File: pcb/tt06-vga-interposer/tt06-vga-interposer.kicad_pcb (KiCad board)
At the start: 2 copper layers, 55.9 x 53.3 mm, 69 parts, among them CON1 Bottom pins, CON2 Bottom pins, CON3 Top socket, CON4 Top socket, J1 Conn_02x07_Odd_Even, J2 DE15_Receptacle_HighDensity_M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, J3 Conn_01x04_Pin, J4 Conn_01x04_Pin, U1 OPA3355EA, U2 SN74ALVC245DWR

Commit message: Partial layout of interposer PCB
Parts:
- added JP16: SolderJumper_2_Open, Anton Kicad Footprints Lib:SolderJumper-2_tiny_nomask, F.Cu at (88.9, 76.2)
- added JP17: SolderJumper_2_Open, Anton Kicad Footprints Lib:SolderJumper-2_tiny_nomask, F.Cu at (88.9, 81.3)
- added U3: SN74LVC245APW, Anton Kicad Footprints Lib:TSSOP-20_4.4x6.5mm_P0.65mm_HandSolder, F.Cu at (241.0, 68.2)
- C1, C2, JP10, JP11, JP12, JP7, JP8, JP9: moved to B.Cu
- J1: value Conn_02x07_Odd_Even -> Conn_02x09_Odd_Even; footprint Connector_PinHeader_2.54mm:PinHeader_2x07_P2.54mm_Vertical -> Connector_PinHeader_2.54mm:PinHeader_2x09_P2.54mm_Horizontal
- moved U2 147.3 mm to (249.3, 69.2)
- moved J1 133.6 mm to (90.2, 48.3), turned to 90 degrees
- moved TP2 115.8 mm to (92.1, 71.1)
- moved TP3 114.9 mm to (92.7, 83.8)
- moved R304 104.8 mm to (91.4, 89.5), turned to -90 degrees
- moved JP301 104.6 mm to (103.5, 80.0), turned to 180 degrees
- moved R305 100.7 mm to (95.2, 89.5), turned to -90 degrees
- moved NT1 100.6 mm to (112.4, 50.8)
- moved R306 100.6 mm to (102.2, 76.2)
- moved R307 100.0 mm to (102.2, 72.4)
- moved R301 99.4 mm to (96.5, 72.4), turned to 180 degrees
- moved R302 99.4 mm to (96.5, 76.2), turned to 180 degrees
- moved R303 99.4 mm to (96.5, 80.0), turned to 180 degrees
- moved R201 98.9 mm to (90.8, 66.7), turned to 180 degrees
- moved JP101 97.2 mm to (113.0, 96.5), turned to 90 degrees
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- renumbered C9 to C3, C11 to C4, C10 to C5, JP16 to JP201, JP17 to JP301, R310 to R1, R309 to R2, R308 to R3, R35 to R4, R33 to R5
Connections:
- J1 pad 13: GND -> inv_aout
- J1 pad 14: GND -> inv_aout
- JP18 pad 2: Net-(JP18-B) -> /hs_buf
- JP19 pad 2: Net-(JP18-B) -> /vs_buf
- R1 pad 1: Net-(U2-B0) -> /hs_buf
- R2 pad 1: Net-(U2-B0) -> /hs_buf
- R3 pad 1: Net-(JP18-B) -> /vs_buf
- R4 pad 1: Net-(JP18-B) -> /vs_buf
- U2 pad 17: Net-(JP18-B) -> /vs_buf
- U2 pad 18: Net-(U2-B0) -> /hs_buf
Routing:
- net GND: track 181.5 -> 344.2 mm, vias 0 -> 1
- net red_out: track 0.00 -> 106.8 mm, vias 0 -> 1
- net blue_out: track 0.00 -> 104.9 mm, vias 0 -> 3
- net green_out: track 0.00 -> 92.2 mm
- net VCC: track 0.00 -> 80.9 mm, vias 0 -> 2
- net dac4_aout: track 0.00 -> 51.6 mm, vias 0 -> 3
- net inv_aout: track 0.00 -> 45.9 mm, vias 0 -> 2
- net red_in: track 0.00 -> 29.6 mm
- net green_in: track 0.00 -> 28.6 mm
- net blue_in: track 0.00 -> 28.5 mm, vias 0 -> 1
- net Net-(U1B--): track 0.00 -> 25.6 mm
- net Net-(R203-Pad2): track 0.00 -> 23.4 mm
- net Net-(R303-Pad2): track 0.00 -> 16.6 mm, vias 0 -> 2
- net vdda_in: track 0.00 -> 15.4 mm
- net Net-(U1C--): track 0.00 -> 12.1 mm, vias 0 -> 2
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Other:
- board size 55.9 x 53.3 mm -> 67.9 x 62.2 mm
- board text added: "B"
- board text added: "G"
- board text added: "R"
- board text added: "dac4_aout"
- board text added: "inv_aout"

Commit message: Nearly finished 1st draft of interposer PCB
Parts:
- removed the JP13 at (88.9, 86.4)
- removed the JP14 at (88.9, 73.7)
- removed the U2 at (249.3, 69.2)
- added J5: Conn_02x07_Odd_Even, Connector_PinHeader_2.54mm:PinHeader_2x07_P2.54mm_Horizontal, F.Cu at (105.4, 96.5)
- added JP16: SolderJumper_2_Open, Anton Kicad Footprints Lib:SolderJumper-2_tiny_nomask, F.Cu at (93.7, 55.9)
- added NT2: NetTie_2, NetTie:NetTie-2_SMD_Pad0.5mm, F.Cu at (91.2, 57.9)
- added NT3: NetTie_2, NetTie:NetTie-2_SMD_Pad0.5mm, F.Cu at (91.2, 59.4)
- C3, C4: moved to B.Cu
- moved U2 140.6 mm to (100.8, 56.4)
- moved JP18 97.8 mm to (100.6, 55.9)
- moved JP17 97.6 mm to (100.6, 54.4)
- moved C4 62.7 mm to (99.2, 58.4)
- moved C3 59.3 mm to (99.2, 54.6)
- moved R4 57.5 mm to (108.0, 58.9), turned to 90 degrees
- moved R3 37.5 mm to (111.3, 58.9), turned to 90 degrees
- moved JP15 29.9 mm to (93.7, 54.4), turned to 180 degrees
- moved R2 28.5 mm to (111.3, 52.8), turned to 90 degrees
- moved R1 27.4 mm to (108.0, 52.8), turned to 90 degrees
- moved R201 26.3 mm to (99.7, 91.4), turned to -90 degrees
- moved R301 19.1 mm to (95.9, 91.4), turned to -90 degrees
- moved R304 18.0 mm to (92.1, 71.5), turned to 90 degrees
- moved R305 18.0 mm to (95.9, 71.5), turned to 90 degrees
- moved TP2 17.6 mm to (99.7, 87.0)
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- renumbered JP16 to JP13, JP17 to JP14, JP18 to JP17, JP19 to JP18, U3 to U2
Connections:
- net vsync_in renamed Net-(JP16-A)
- J1 pad 1: VCC -> GND
- J1 pad 10: hsync_out -> vsync_out
- J1 pad 11: vsync_out -> blue_out
- J1 pad 12: vsync_out -> blue_out
- J1 pad 13: inv_aout -> green_out
- J1 pad 14: inv_aout -> green_out
- J1 pad 15: dac4_aout -> red_out
- J1 pad 16: dac4_aout -> red_out
- J1 pad 17: GND -> VCC
- J1 pad 18: GND -> VCC
- J1 pad 2: VCC -> GND
- J1 pad 3: red_out -> inv_aout
- J1 pad 4: red_out -> inv_aout
- J1 pad 5: green_out -> dac4_aout
- J1 pad 6: green_out -> dac4_aout
- J1 pad 7: blue_out -> hsync_out
- J1 pad 8: blue_out -> hsync_out
- J1 pad 9: hsync_out -> vsync_out
- JP15 pad 1: /chip_an4 -> Net-(JP15-A)
- JP15 pad 2: blue_in -> hsync_in
- JP17 pad 1: hsync_in -> Net-(JP15-A)
- U2 pad 2: hsync_in -> Net-(JP15-A)
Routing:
- net GND: track 344.2 -> 595.6 mm, vias 1 -> 10
- net hsync_out: track 2.54 -> 67.8 mm
- net vsync_out: track 2.54 -> 64.8 mm, vias 0 -> 1
- net /chip_an0: track 7.27 -> 46.5 mm, vias 0 -> 1
- net red_out: track 106.8 -> 75.9 mm
- net green_out: track 92.2 -> 63.3 mm
- net /chip_an5: track 7.27 -> 33.5 mm, vias 0 -> 1
- net /chip_an4: track 7.27 -> 32.4 mm, vias 0 -> 1
- net blue_out: track 104.9 -> 81.3 mm, vias 3 -> 1
- net Net-(U1B--): track 25.6 -> 7.58 mm
- net dac4_aout: track 51.6 -> 37.9 mm, vias 3 -> 1
- net /vs_buf: track 0.00 -> 13.5 mm
- net red_in: track 29.6 -> 16.3 mm
- net inv_aout: track 45.9 -> 32.9 mm, vias 2 -> 1
- net /hs_buf: track 0.00 -> 10.4 mm
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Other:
- board size 67.9 x 62.2 mm -> 67.3 x 62.2 mm

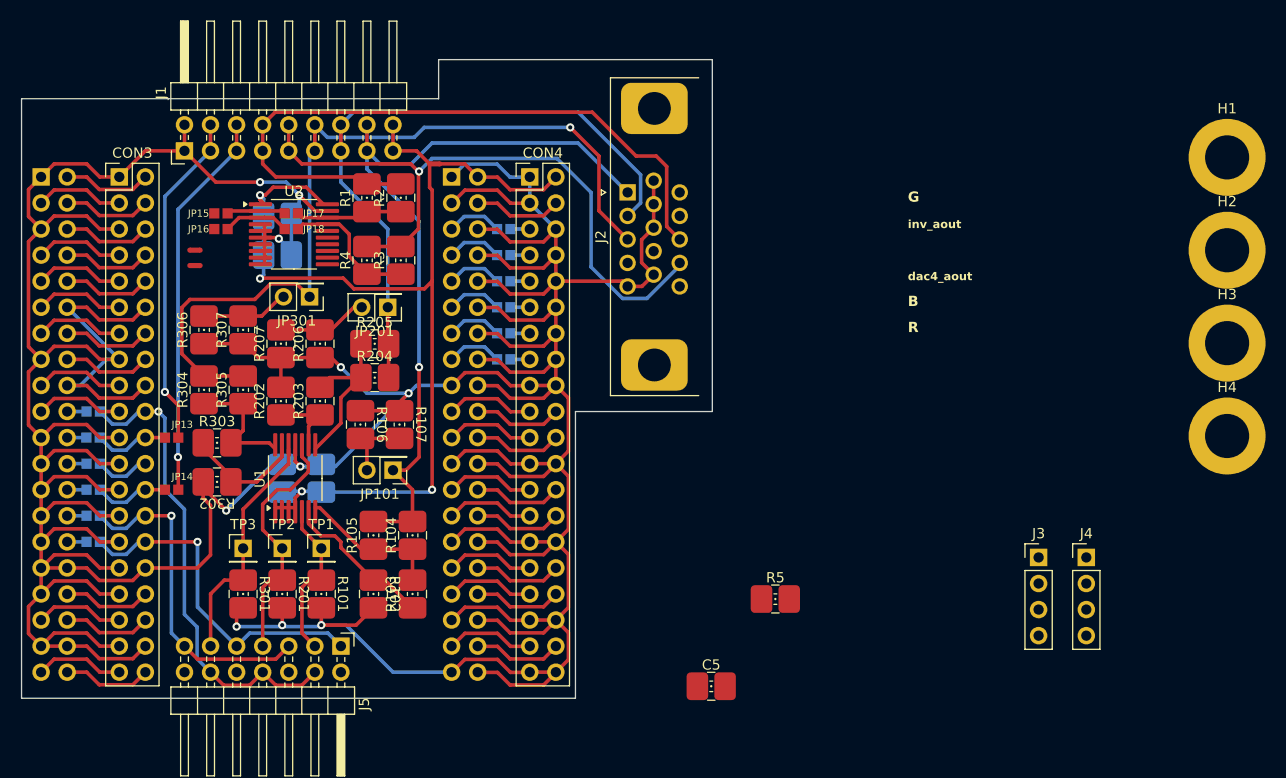
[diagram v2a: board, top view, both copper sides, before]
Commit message: Interposer PCB: First complete version
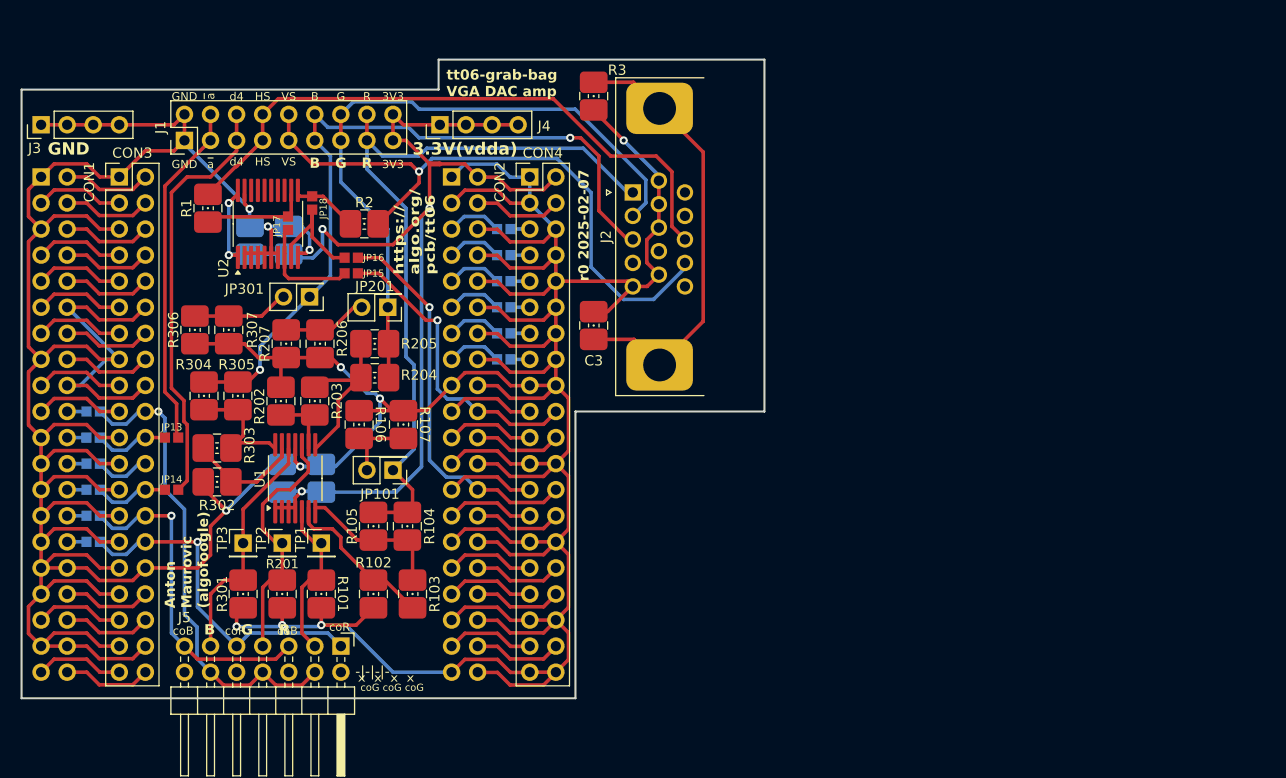
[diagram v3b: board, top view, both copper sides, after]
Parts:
- removed H1, H2, H3, H4: MountingHole, MountingHole:MountingHole_4.3mm_M4_DIN965_Pad
- removed NT2, NT3: NetTie_2, NetTie:NetTie-2_SMD_Pad0.5mm
- removed the R3 at (111.3, 58.9)
- removed R4: 100, Anton Kicad Footprints Lib:SMD_Passive_HandSolder_0603_to_1210
- J1: footprint Connector_PinHeader_2.54mm:PinHeader_2x09_P2.54mm_Horizontal -> Connector_PinHeader_2.54mm:PinHeader_2x09_P2.54mm_Vertical
- R1, R2: value 100 -> 49.9
- moved J3 105.9 mm to (76.2, 45.7), turned to 90 degrees
- moved J4 75.8 mm to (115.1, 45.7), turned to 90 degrees
- moved R3 52.1 mm to (130.0, 42.9), turned to -90 degrees
- moved C3 37.0 mm to (130.0, 65.3), turned to 90 degrees
- moved R1 15.5 mm to (92.5, 53.8)
- moved JP15 14.0 mm to (106.4, 60.2), turned to 0 degrees
- moved JP16 13.0 mm to (106.4, 58.7), turned to 0 degrees
- moved R2 4.37 mm to (107.7, 55.4), turned to 0 degrees
- moved C4 3.56 mm to (96.6, 57.0), turned to 90 degrees
- moved JP18 3.25 mm to (102.6, 53.3), turned to 90 degrees
- moved U2 2.74 mm to (98.3, 55.4), turned to 90 degrees
- moved C5 1.81 mm to (100.3, 57.0), turned to 90 degrees
- moved R307 1.40 mm to (94.5, 65.7)
- moved R104 1.02 mm to (111.9, 84.8)
- moved J1 1.02 mm to (90.2, 47.2)
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- renumbered C5 to C3, C3 to C4, C4 to C5, R5 to R3
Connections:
- JP15 pad 1: Net-(JP15-A) -> hsync_in
- JP15 pad 2: hsync_in -> /uout7
- JP16 pad 1: Net-(JP16-A) -> vsync_in
- JP16 pad 2: vsync_in -> /uout3
- JP17 pad 1: Net-(JP15-A) -> hsync_in
- JP18 pad 1: Net-(JP16-A) -> vsync_in
- R2 pad 1: /hs_buf -> /vs_buf
- R2 pad 2: hsync_out -> vsync_out
- U2 pad 11: unconnected-(U2-B8-Pad11) -> /vs_buf
- U2 pad 12: unconnected-(U2-B7-Pad12) -> /hs_buf
- U2 pad 17: /vs_buf -> unconnected-(U2-B2-Pad17)
- U2 pad 18: /hs_buf -> unconnected-(U2-B1-Pad18)
- U2 pad 2: Net-(JP15-A) -> GND
- U2 pad 3: Net-(JP16-A) -> GND
- U2 pad 8: GND -> hsync_in
- U2 pad 9: GND -> vsync_in
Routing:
- net Net-(C3-Pad1): track 0.00 -> 43.4 mm
- net /uout3: track 8.63 -> 38.4 mm, vias 0 -> 1
- net GND: track 595.6 -> 620.1 mm, vias 10 -> 11
- net /uout7: track 8.63 -> 29.8 mm, vias 0 -> 1
- net vsync_in: track 0.00 -> 11.7 mm
- net hsync_in: track 0.00 -> 10.7 mm
- net VCC: track 91.2 -> 99.4 mm, vias 4 -> 5
- net blue_out: track 81.3 -> 73.5 mm, vias 1 -> 2
- net /vs_buf: track 13.5 -> 6.31 mm
- net hsync_out: track 67.8 -> 60.6 mm
- net Net-(JP16-A): track 6.48 -> 0.00 mm
- net Net-(JP15-A): track 5.76 -> 0.00 mm
- net dac4_aout: track 37.9 -> 41.5 mm, vias 1 -> 0
- net vsync_out: track 64.8 -> 61.4 mm
- net green_out: track 63.3 -> 65.0 mm
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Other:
- board size 67.3 x 62.2 mm -> 72.4 x 62.2 mm
- board text added: "-|-|-|-"
- board text added: "3.3V(vdda)"
- board text added: "3V3"
- board text added: "Anton Maurovic (algofoogle)"
- board text added: "B G R"
- board text added: "GND"
- board text added: "HS"
- board text added: "Mousebites for VGA breakout?"
- board text added: "Round corners"
- board text added: "Thicker power/ground traces?"
- board text added: "VS"
- board text added: "coB"
- board text added: "coG coG coG"
- board text added: "coR"
- board text added: "d4"
- board text added: "https:// algo.org/ pcb/tt06"
- board text added: "r0 2025-02-07"
- board text added: "tt06-grab-bag VGA DAC amp"
- board text added: "x x x x"
- board text added: "~{a}"
- board text removed: "dac4_aout"
- board text removed: "inv_aout"

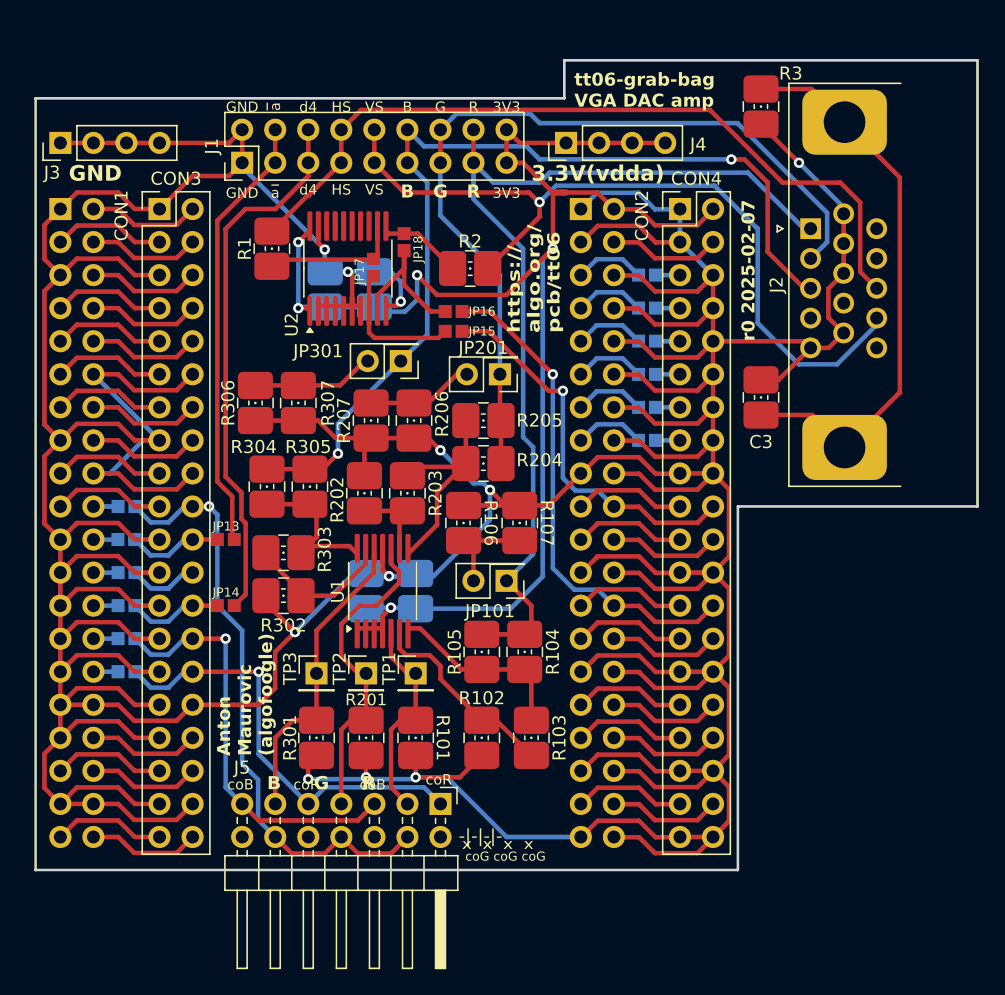
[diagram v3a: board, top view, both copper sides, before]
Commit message: Interposer PCB: Rounded corners
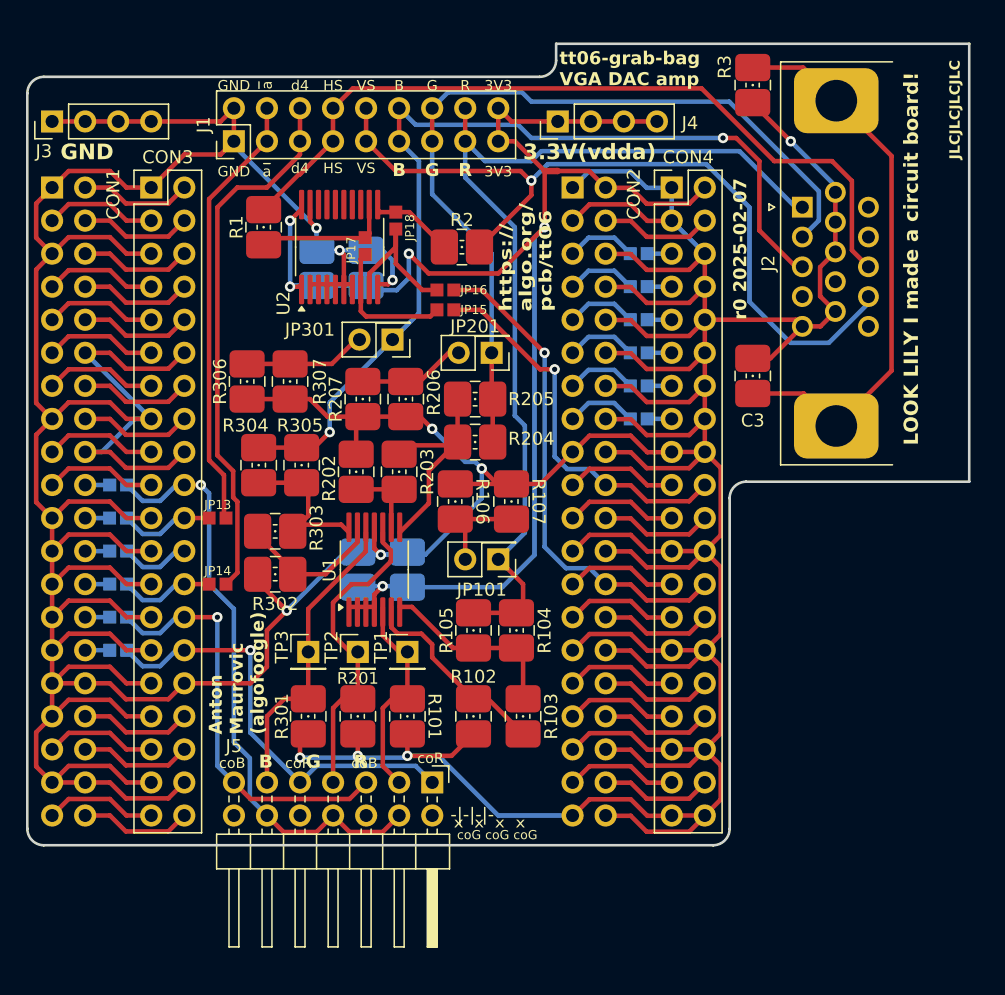
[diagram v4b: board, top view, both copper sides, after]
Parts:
- moved R106 1.77 mm to (106.6, 73.3)
- moved R107 1.77 mm to (110.9, 73.3)
- moved R203 1.77 mm to (102.2, 71.0)
- moved R204 1.77 mm to (108.1, 68.7)
- moved U1 1.77 mm to (100.3, 78.5)
- moved C1 1.77 mm to (99.1, 78.5)
- moved C2 1.77 mm to (102.9, 78.5)
- moved JP8 1.77 mm to (120.7, 64.4)
- moved R202 1.77 mm to (98.9, 71.0)
- moved JP15 1.77 mm to (105.8, 58.5)
- moved JP18 1.77 mm to (102.0, 51.7)
- moved JP201 1.77 mm to (109.3, 61.8)
- moved NT1 1.77 mm to (113.9, 47.9)
- moved U2 1.77 mm to (97.7, 53.7)
- moved C3 1.77 mm to (129.4, 63.6)
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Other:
- board size 72.4 x 62.2 mm -> 72.4 x 61.6 mm
- board text added: "JLCJLCJLCJLC"
- board text added: "LOOK LILY I made a circuit board!"
- board text removed: "Round corners"

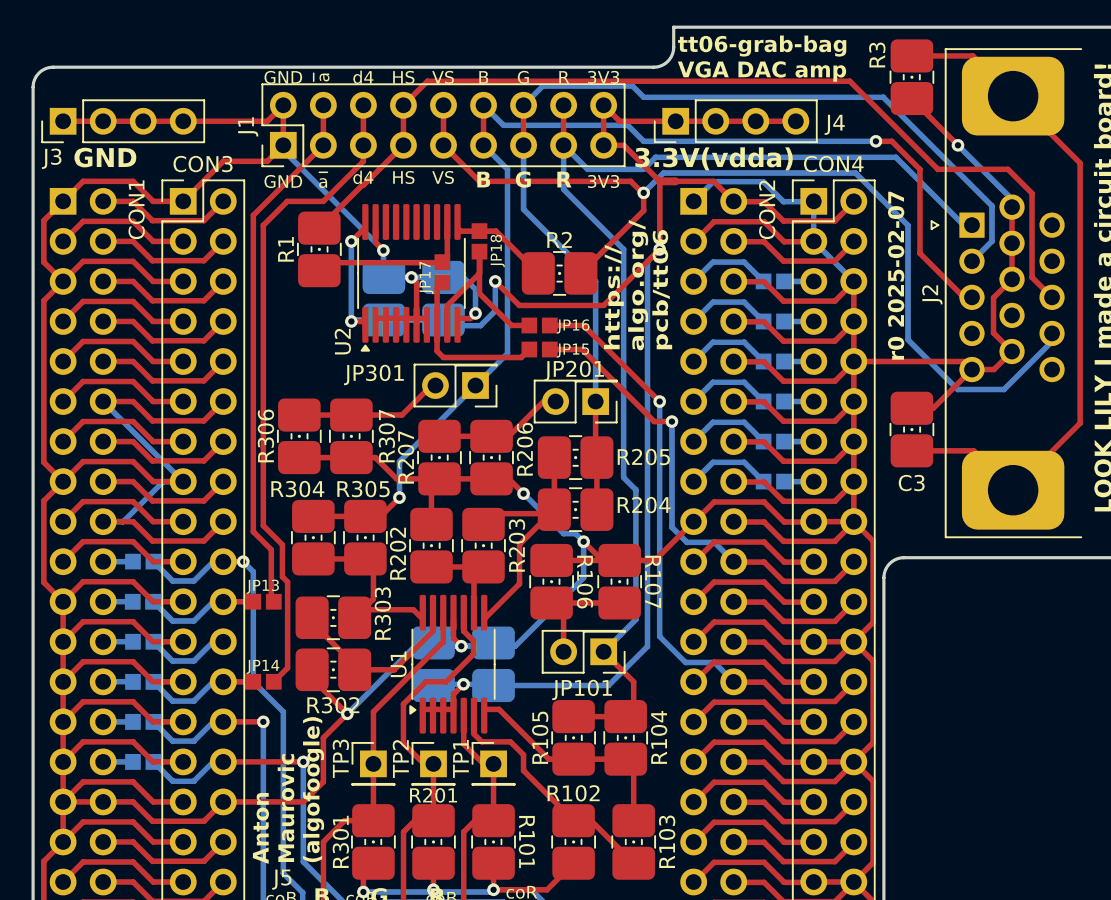
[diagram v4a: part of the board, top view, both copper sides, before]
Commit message: Interposer PCB: Thicken power traces, add final Gerbers
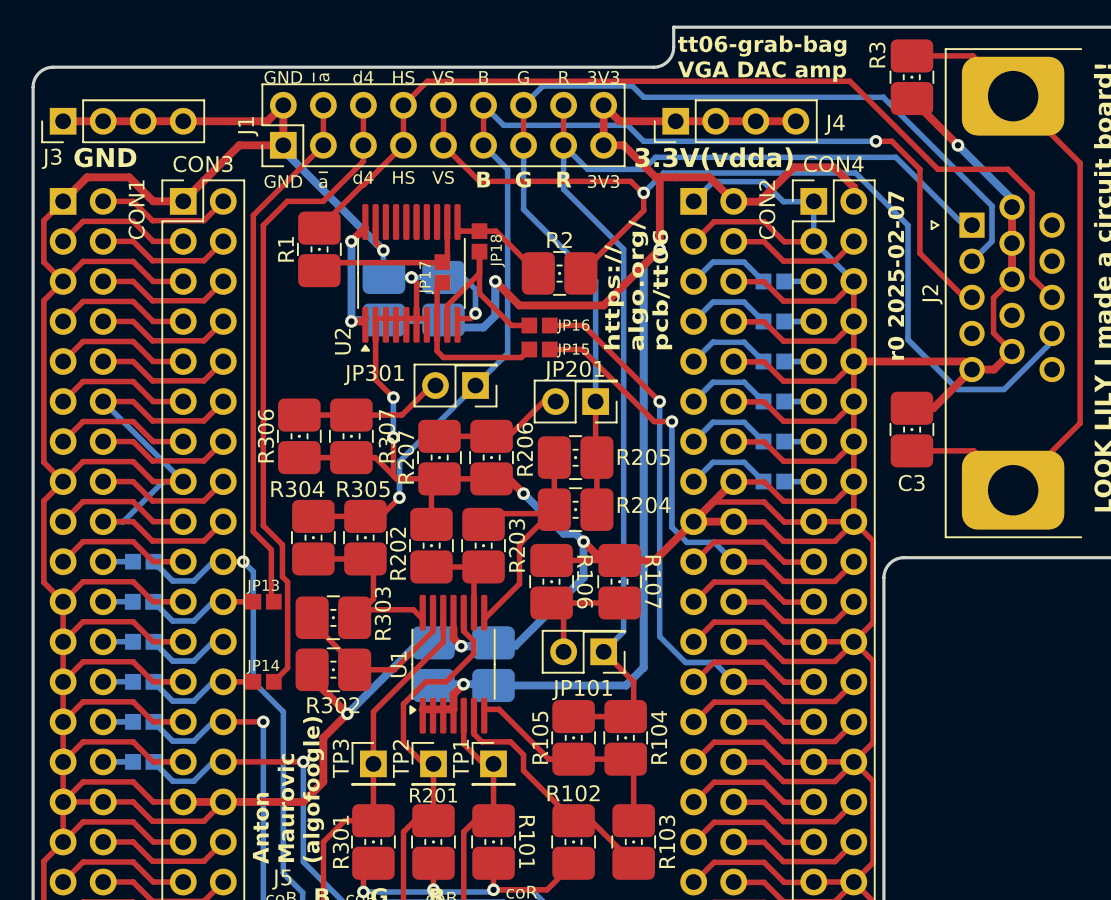
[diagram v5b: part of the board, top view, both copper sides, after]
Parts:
- moved NT1 0.25 mm to (113.9, 47.6)
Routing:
- net GND: track 620.1 -> 639.1 mm, vias 11 -> 13
- net vdda_in: track 12.8 -> 14.3 mm
- net VCC: track 99.4 -> 100.4 mm
- net red_out: track 74.5 -> 73.8 mm
